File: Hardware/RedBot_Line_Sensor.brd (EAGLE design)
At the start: 7.6 x 24.1 mm, 9 parts, among them U1 QRE1113

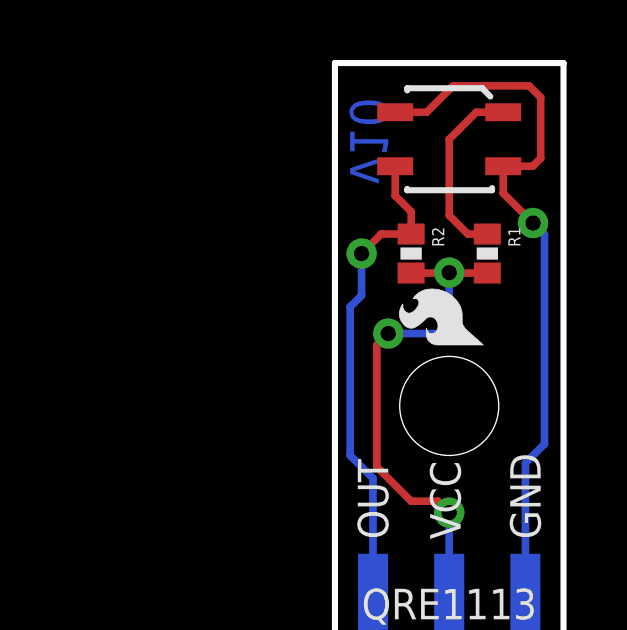
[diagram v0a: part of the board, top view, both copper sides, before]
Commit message: Production Readied
Added fiducial reference points & created panel for manufacture.
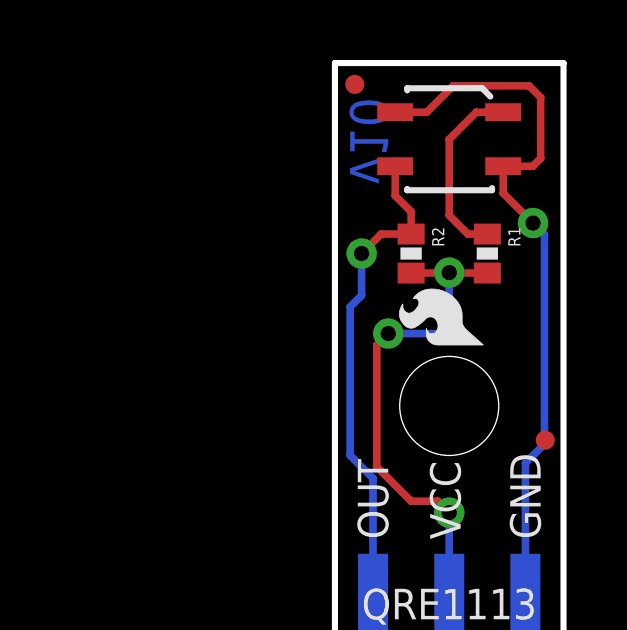
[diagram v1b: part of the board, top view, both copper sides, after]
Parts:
- added FID1, FID2: FIDUCIALUFIDUCIAL, SparkFun-Aesthetics:MICRO-FIDUCIAL
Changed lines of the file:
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@@
 <setting verticaltext="up"/>
 </settings>
-<grid distance="0.05" unitdist="inch" unit="inch" style="lines" multiple="1" display="yes" altdistance="0.005" altunitdist="inch" altunit="inch"/>
+<grid distance="0.001" unitdist="inch" unit="inch" style="lines" multiple="1" display="yes" altdistance="0.01" altunitdist="inch" altunit="inch"/>
 <layers>
 <layer number="1" name="Top" color="4" fill="1" visible="yes" active="yes"/>
-<layer number="2" name="Route2" color="1" fill="3" visible="no" active="yes"/>
-<layer number="15" name="Route15" color="4" fill="6" visible="no" active="yes"/>
+<layer number="2" name="Route2" color="1" fill="3" visible="yes" active="yes"/>
+<layer number="15" name="Route15" color="4" fill="6" visible="yes" active="yes"/>
 <layer number="16" name="Bottom" color="1" fill="1" visible="yes" active="yes"/>
 <layer number="17" name="Pads" color="2" fill="1" visible="yes" active="yes"/>
 <layer number="18" name="Vias" color="2" fill="1" visible="yes" active="yes"/>
 <layer number="19" name="Unrouted" color="6" fill="1" visible="yes" active="yes"/>
-<layer number="20" name="Dimension" color="15" fill="1" visible="yes" active="yes"/>
-<layer number="21" name="tPlace" color="16" fill="1" visible="yes" active="yes"/>
-<layer number="22" name="bPlace" color="14" fill="1" visible="yes" active="yes"/>
+<layer number="20" name="Dimension" color="6" fill="1" visible="yes" active="yes"/>
+<layer number="21" name="tPlace" color="6" fill="1" visible="yes" active="yes"/>
+<layer number="22" name="bPlace" color="6" fill="1" visible="yes" active="yes"/>
 <layer number="23" name="tOrigins" color="15" fill="1" visible="yes" active="yes"/>
 <layer number="24" name="bOrigins" color="15" fill="1" visible="yes" active="yes"/>
-<layer number="25" name="tNames" color="7" fill="1" visible="no" active="yes"/>
-<layer number="26" name="bNames" color="7" fill="1" visible="no" active="yes"/>
-<layer number="27" name="tValues" color="7" fill="1" visible="no" active="yes"/>
-<layer number="28" name="bValues" color="7" fill="1" visible="no" active="yes"/>
-<layer number="29" name="tStop" color="7" fill="3" visible="no" active="yes"/>
-<layer number="30" name="bStop" color="7" fill="6" visible="no" active="yes"/>
-<layer number="31" name="tCream" color="7" fill="4" visible="no" active="yes"/>
-<layer number="32" name="bCream" color="7" fill="5" visible="no" active="yes"/>
-<layer number="39" name="tKeepout" color="4" fill="11" visible="no" active="yes"/>
-<layer number="40" name="bKeepout" color="1" fill="11" visible="no" active="yes"/>
-<layer number="41" name="tRestrict" color="4" fill="10" visible="no" active="yes"/>
-<layer number="42" name="bRestrict" color="1" fill="10" visible="no" active="yes"/>
-<layer number="44" name="Drills" color="7" fill="1" visible="no" active="yes"/>
+<layer number="25" name="tNames" color="7" fill="1" visible="yes" active="yes"/>
+<layer number="26" name="bNames" color="7" fill="1" visible="yes" active="yes"/>
+<layer number="27" name="tValues" color="7" fill="1" visible="yes" active="yes"/>
+<layer number="28" name="bValues" color="7" fill="1" visible="yes" active="yes"/>
+<layer number="29" name="tStop" color="7" fill="3" visible="yes" active="yes"/>
+<layer number="30" name="bStop" color="7" fill="6" visible="yes" active="yes"/>
+<layer number="31" name="tCream" color="7" fill="4" visible="yes" active="yes"/>
+<layer number="32" name="bCream" color="7" fill="5" visible="yes" active="yes"/>
+<layer number="39" name="tKeepout" color="4" fill="11" visible="yes" active="yes"/>
+<layer number="40" name="bKeepout" color="1" fill="11" visible="yes" active="yes"/>
+<layer number="41" name="tRestrict" color="4" fill="10" visible="yes" active="yes"/>
+<layer number="42" name="bRestrict" color="1" fill="10" visible="yes" active="yes"/>
+<layer number="44" name="Drills" color="7" fill="1" visible="yes" active="yes"/>
 <layer number="45" name="Holes" color="7" fill="1" visible="yes" active="yes"/>
-<layer number="46" name="Milling" color="3" fill="1" visible="no" active="yes"/>
+<layer number="46" name="Milling" color="3" fill="1" visible="yes" active="yes"/>
 <layer number="51" name="tDocu" color="6" fill="1" visible="yes" active="yes"/>
-<layer number="52" name="bDocu" color="7" fill="1" visible="no" active="yes"/>
+<layer number="52" name="bDocu" color="7" fill="1" visible="yes" active="yes"/>
 <layer number="3" name="Route3" color="4" fill="3" visible="no" active="no"/>
 <layer number="4" name="Route4" color="1" fill="4" visible="no" active="no"/>
@@
 <element name="STANDOFF1" library="SparkFun-Electromechanical" package="STAND-OFF" value="STAND-OFF" x="3.81" y="12.7"/>
 <element name="LOGO3" library="SparkFun-Aesthetics" package="SFE-LOGO-FLAME" value="LOGO-SFESK" x="4.826" y="17.272" rot="MR0"/>
+<element name="FID1" library="SparkFun-Aesthetics" package="MICRO-FIDUCIAL" value="FIDUCIALUFIDUCIAL" x="7.0104" y="11.557"/>
+<element name="FID2" library="SparkFun-Aesthetics" package="MICRO-FIDUCIAL" value="FIDUCIALUFIDUCIAL" x="0.6604" y="23.4188"/>
 </elements>
 <signals>

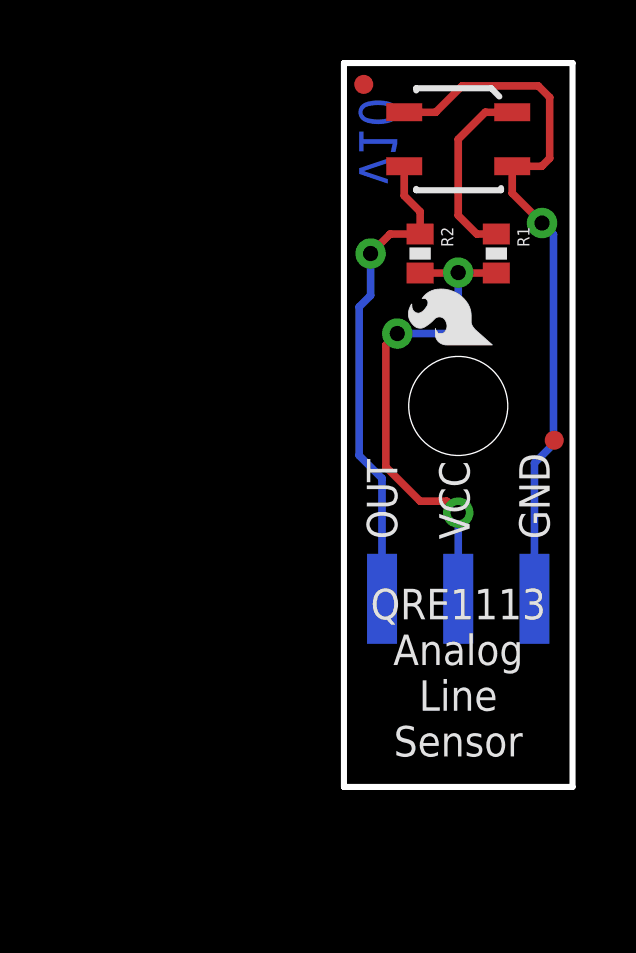
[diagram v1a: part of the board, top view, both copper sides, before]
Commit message: QC Revision
Changes:
1.) 0402 to 0603 footprint
2.) Updated QRE1113 footprint
3.) New 3-pin SMD header footprint w/ bosses
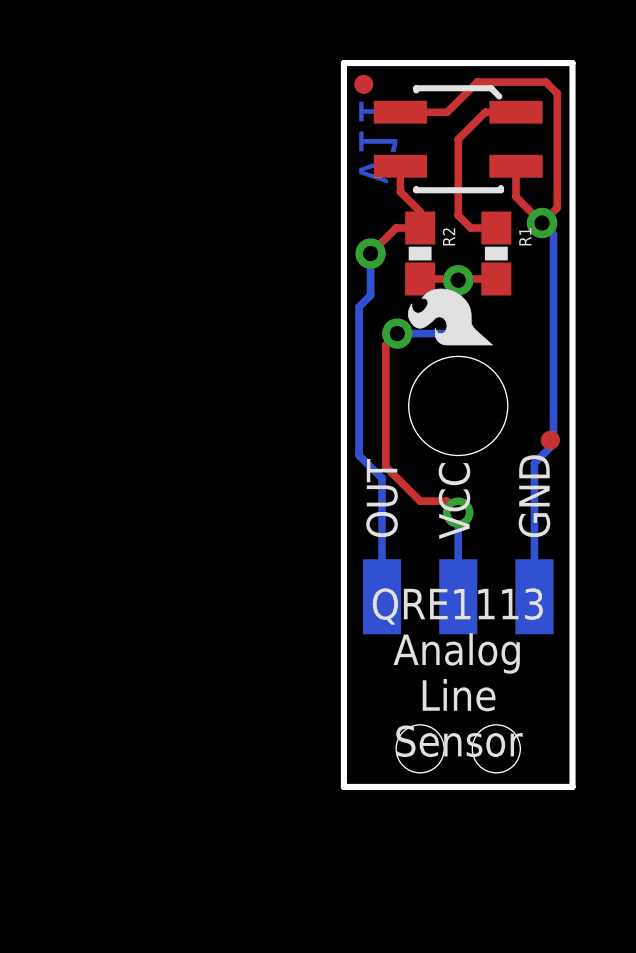
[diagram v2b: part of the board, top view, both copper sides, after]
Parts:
- JP1: device SparkFun-Connectors:1X03_SMD_RA_MALE -> SparkFun-Connectors:1X03_SMD_RA_MALE_POST
- R1, R2: device SparkFun-Resistors:0402-RES -> SparkFun-Resistors:0603-RES
- U1: value QRE1113 -> QRE1113SMD-W; device SparkFun-Sensors:QRE1113 -> SparkFun-Sensors:QRE1113-W
- moved FID1 0.13 mm to (6.88, 11.6)
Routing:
- net GND: track 24.0 -> 25.5 mm
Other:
- board text added: "v11"
- board text removed: "v10"

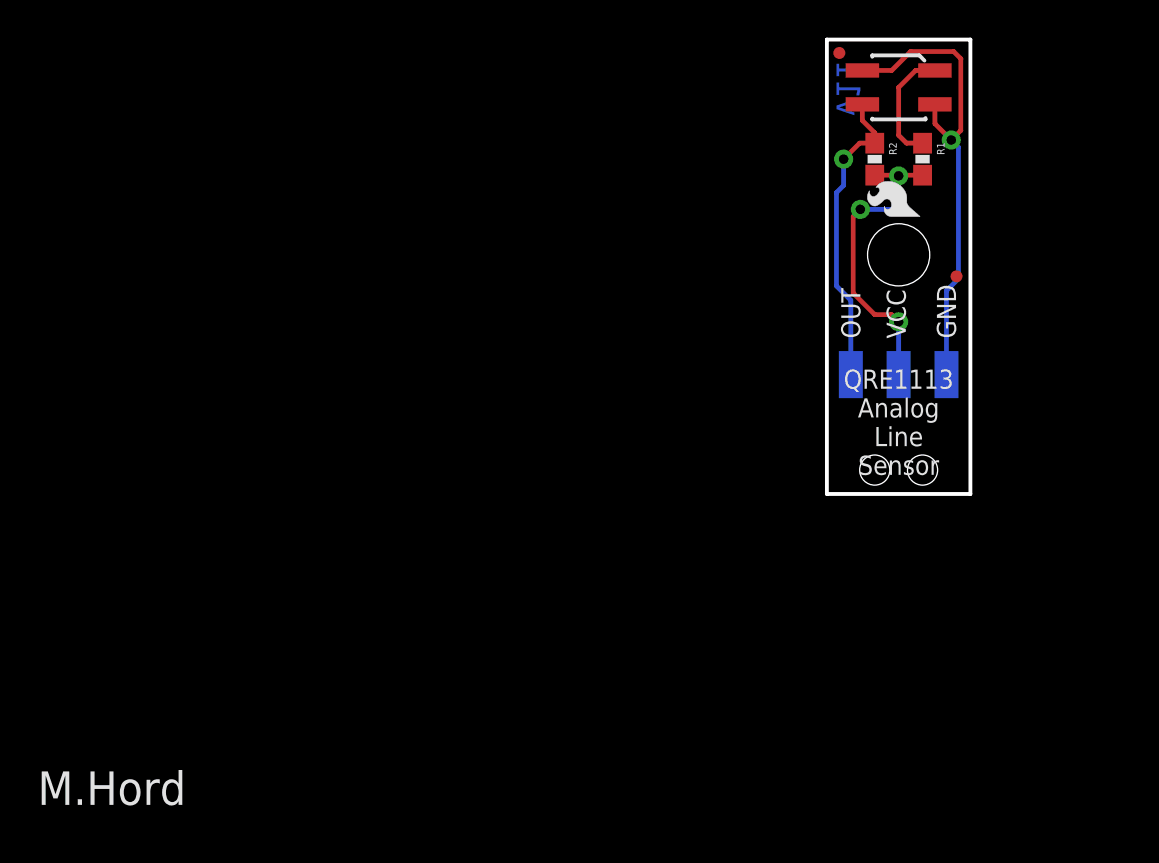
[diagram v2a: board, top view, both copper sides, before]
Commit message: Minor aesthetic fixes
1.) Moved VCC via away from silk
2.) Moved board name silk away from header boss holes
3.) Updated version info in schematic.
4.) Moved flame on top side out to avoid resistor tcreme.
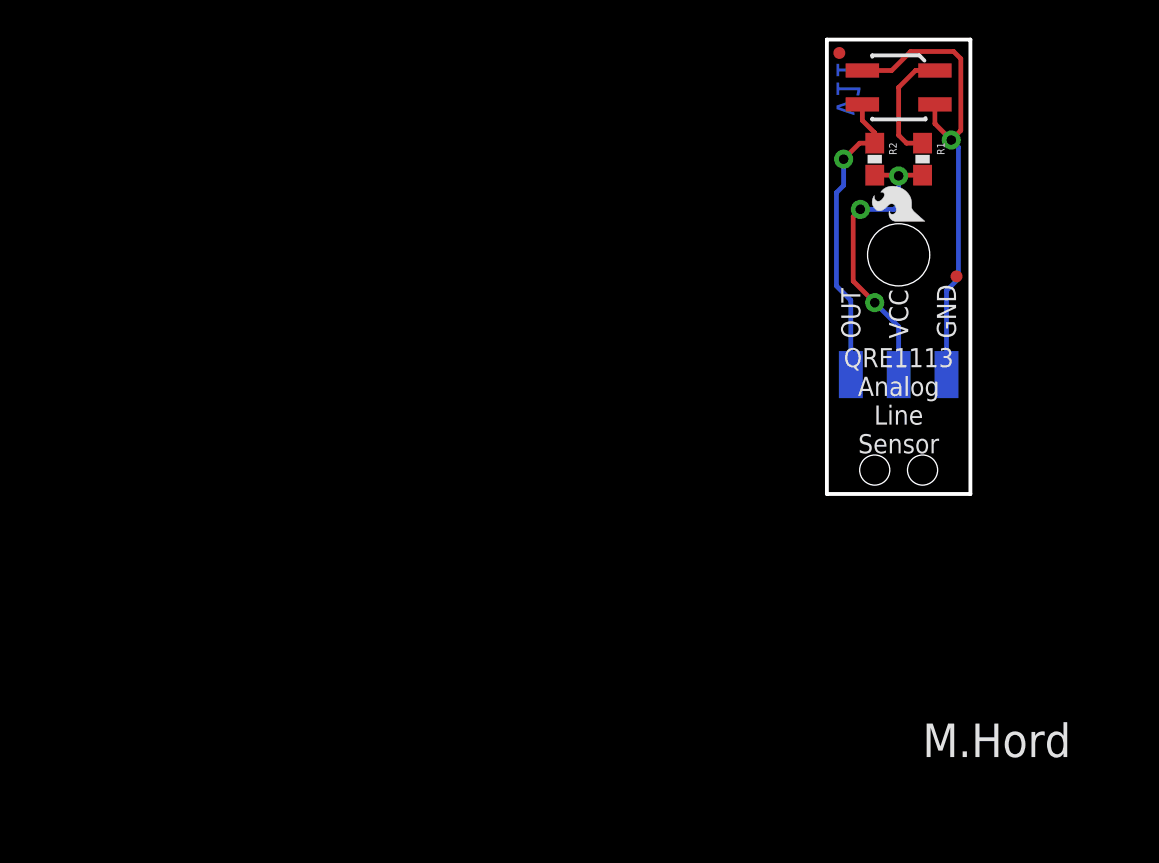
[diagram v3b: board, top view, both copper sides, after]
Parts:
- moved FRAME1 47.1 mm to (-25.4, -14.0)
- moved LOGO1 0.36 mm to (5.21, 14.5)
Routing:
- net 5V: track 16.7 -> 16.2 mm
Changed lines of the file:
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@@
 <?xml version="1.0" encoding="utf-8"?>
 <!DOCTYPE eagle SYSTEM "eagle.dtd">
-<eagle version="6.5.0">
+<eagle version="6.4">
 <drawing>
 <settings>
@@
 <layers>
 <layer number="1" name="Top" color="4" fill="1" visible="yes" active="yes"/>
-<layer number="2" name="Route2" color="1" fill="3" visible="no" active="yes"/>
-<layer number="15" name="Route15" color="4" fill="6" visible="no" active="yes"/>
+<layer number="2" name="Route2" color="1" fill="3" visible="yes" active="yes"/>
+<layer number="15" name="Route15" color="4" fill="6" visible="yes" active="yes"/>
 <layer number="16" name="Bottom" color="1" fill="1" visible="yes" active="yes"/>
 <layer number="17" name="Pads" color="2" fill="1" visible="yes" active="yes"/>
@@
 <layer number="23" name="tOrigins" color="15" fill="1" visible="yes" active="yes"/>
 <layer number="24" name="bOrigins" color="15" fill="1" visible="yes" active="yes"/>
-<layer number="25" name="tNames" color="7" fill="1" visible="no" active="yes"/>
-<layer number="26" name="bNames" color="7" fill="1" visible="no" active="yes"/>
-<layer number="27" name="tValues" color="7" fill="1" visible="no" active="yes"/>
-<layer number="28" name="bValues" color="7" fill="1" visible="no" active="yes"/>
-<layer number="29" name="tStop" color="7" fill="3" visible="no" active="yes"/>
-<layer number="30" name="bStop" color="7" fill="6" visible="no" active="yes"/>
-<layer number="31" name="tCream" color="7" fill="4" visible="no" active="yes"/>
-<layer number="32" name="bCream" color="7" fill="5" visible="no" active="yes"/>
-<layer number="39" name="tKeepout" color="4" fill="11" visible="no" active="yes"/>
-<layer number="40" name="bKeepout" color="1" fill="11" visible="no" active="yes"/>
-<layer number="41" name="tRestrict" color="4" fill="10" visible="no" active="yes"/>
-<layer number="42" name="bRestrict" color="1" fill="10" visible="no" active="yes"/>
-<layer number="44" name="Drills" color="7" fill="1" visible="no" active="yes"/>
+<layer number="25" name="tNames" color="7" fill="1" visible="yes" active="yes"/>
+<layer number="26" name="bNames" color="7" fill="1" visible="yes" active="yes"/>
+<layer number="27" name="tValues" color="7" fill="1" visible="yes" active="yes"/>
+<layer number="28" name="bValues" color="7" fill="1" visible="yes" active="yes"/>
+<layer number="29" name="tStop" color="7" fill="3" visible="yes" active="yes"/>
+<layer number="30" name="bStop" color="7" fill="6" visible="yes" active="yes"/>
+<layer number="31" name="tCream" color="7" fill="4" visible="yes" active="yes"/>
+<layer number="32" name="bCream" color="7" fill="5" visible="yes" active="yes"/>
+<layer number="39" name="tKeepout" color="4" fill="11" visible="yes" active="yes"/>
+<layer number="40" name="bKeepout" color="1" fill="11" visible="yes" active="yes"/>
+<layer number="41" name="tRestrict" color="4" fill="10" visible="yes" active="yes"/>
+<layer number="42" name="bRestrict" color="1" fill="10" visible="yes" active="yes"/>
+<layer number="44" name="Drills" color="7" fill="1" visible="yes" active="yes"/>
 <layer number="45" name="Holes" color="7" fill="1" visible="yes" active="yes"/>
-<layer number="46" name="Milling" color="3" fill="1" visible="no" active="yes"/>
+<layer number="46" name="Milling" color="3" fill="1" visible="yes" active="yes"/>
 <layer number="51" name="tDocu" color="6" fill="1" visible="yes" active="yes"/>
-<layer number="52" name="bDocu" color="7" fill="1" visible="no" active="yes"/>
+<layer number="52" name="bDocu" color="7" fill="1" visible="yes" active="yes"/>
 <layer number="3" name="Route3" color="4" fill="3" visible="no" active="no"/>
 <layer number="4" name="Route4" color="1" fill="4" visible="no" active="no"/>
@@
 <layer number="106" name="bPlate" color="7" fill="1" visible="no" active="no"/>
 <layer number="107" name="Crop" color="7" fill="1" visible="no" active="no"/>
-<layer number="108" name="tplace-old" color="10" fill="1" visible="no" active="yes"/>
-<layer number="109" name="ref-old" color="11" fill="1" visible="no" active="yes"/>
+<layer number="108" name="tplace-old" color="10" fill="1" visible="yes" active="yes"/>
+<layer number="109" name="ref-old" color="11" fill="1" visible="yes" active="yes"/>
 <layer number="116" name="Patch_BOT" color="9" fill="4" visible="no" active="no"/>
 <layer number="121" name="_tsilk" color="7" fill="1" visible="no" active="no"/>
@@
 <plain>
 <text x="1.27" y="8.255" size="1.016" layer="21" font="vector" ratio="15" rot="R90" align="center-left">OUT</text>
-<text x="3.683" y="8.255" size="1.016" layer="21" font="vector" ratio="15" rot="R90" align="center-left">VCC</text>
+<text x="3.81" y="8.255" size="1.016" layer="21" font="vector" ratio="15" rot="R90" align="center-left">VCC</text>
 <text x="6.35" y="8.255" size="1.016" layer="21" font="vector" ratio="15" rot="R90" align="center-left">GND</text>
 <text x="1.27" y="8.255" size="1.016" layer="22" font="vector" ratio="15" rot="MR90" align="center-left">OUT</text>
-<text x="3.683" y="8.255" size="1.016" layer="22" font="vector" ratio="15" rot="MR90" align="center-left">VCC</text>
+<text x="3.81" y="8.255" size="1.016" layer="22" font="vector" ratio="15" rot="MR90" align="center-left">VCC</text>
 <text x="6.35" y="8.255" size="1.016" layer="22" font="vector" ratio="15" rot="MR90" align="center-left">GND</text>
-<text x="3.81" y="3.81" size="1.016" layer="21" font="vector" ratio="15" align="center">QRE1113
+<text x="3.81" y="4.953" size="1.016" layer="21" font="vector" ratio="15" align="center">QRE1113
 Analog
 Line
@@
 <wire x1="7.62" y1="24.13" x2="0" y2="24.13" width="0.2032" layer="20"/>
 <wire x1="0" y1="24.13" x2="0" y2="0" width="0.2032" layer="20"/>
-<text x="-41.91" y="-16.51" size="1.778" layer="25" font="vector" ratio="15">M.Hord</text>
+<text x="5.08" y="-13.97" size="1.778" layer="25" font="vector" ratio="15">M.Hord</text>
 <text x="0.508" y="20.066" size="1.27" layer="16" font="vector" ratio="20" rot="MR90">v11</text>
 </plain>
@@
 </autorouter>
 <elements>
-<element name="FRAME1" library="SparkFun-Aesthetics" package="CREATIVE_COMMONS" value="FRAME-LETTER" x="-72.39" y="-16.51"/>
-<element name="LOGO1" library="SparkFun-Aesthetics" package="SFE-LOGO-FLAME" value="LOGO-SFESK" x="4.953" y="14.732" rot="R90"/>
+<element name="FRAME1" library="SparkFun-Aesthetics" package="CREATIVE_COMMONS" value="FRAME-LETTER" x="-25.4" y="-13.97"/>
+<element name="LOGO1" library="SparkFun-Aesthetics" package="SFE-LOGO-FLAME" value="LOGO-SFESK" x="5.207" y="14.478" rot="R90"/>
 <element name="LOGO2" library="SparkFun-Aesthetics" package="OSHW-LOGO-S" value="OSHW-LOGOS" x="3.81" y="21.59" rot="MR0"/>
 <element name="U1" library="SparkFun-Sensors" package="QRE1113-W" value="QRE1113SMD-W" x="3.81" y="21.59" rot="R180"/>
@@
 <via x="1.778" y="15.113" extent="1-16" drill="0.508"/>
 <wire x1="1.778" y1="15.113" x2="1.397" y2="14.732" width="0.254" layer="1"/>
-<wire x1="1.397" y1="14.732" x2="1.397" y2="10.668" width="0.254" layer="1"/>
-<wire x1="1.397" y1="10.668" x2="2.54" y2="9.525" width="0.254" layer="1"/>
-<wire x1="2.54" y1="9.525" x2="3.429" y2="9.525" width="0.254" layer="1"/>
-<wire x1="3.429" y1="9.525" x2="3.81" y2="9.144" width="0.254" layer="1"/>
-<wire x1="3.81" y1="9.144" x2="3.81" y2="6.34" width="0.254" layer="16"/>
-<via x="3.81" y="9.144" extent="1-16" drill="0.508"/>
+<via x="2.54" y="10.16" extent="1-16" drill="0.508"/>
 <wire x1="2.54" y1="16.93" x2="3.771" y2="16.93" width="0.254" layer="1"/>
 <wire x1="3.771" y1="16.93" x2="3.81" y2="16.891" width="0.254" layer="1"/>
 <wire x1="5.08" y1="16.93" x2="3.849" y2="16.93" width="0.254" layer="1"/>
 <wire x1="3.849" y1="16.93" x2="3.81" y2="16.891" width="0.254" layer="1"/>
+<wire x1="3.81" y1="6.34" x2="3.81" y2="8.89" width="0.254" layer="16"/>
+<wire x1="3.81" y1="8.89" x2="2.54" y2="10.16" width="0.254" layer="16"/>
+<wire x1="1.397" y1="14.732" x2="1.397" y2="11.303" width="0.254" layer="1"/>
+<wire x1="1.397" y1="11.303" x2="2.54" y2="10.16" width="0.254" layer="1"/>
 </signal>
 <signal name="GND">
